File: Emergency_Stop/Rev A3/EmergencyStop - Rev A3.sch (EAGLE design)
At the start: 12 parts, among them J3 NC3FBV2-SW, J4 NC3MAV, J5 22-05-7038-03, J6 22-05-7028-02, T1 EXMACHINA-LOGO-NAME

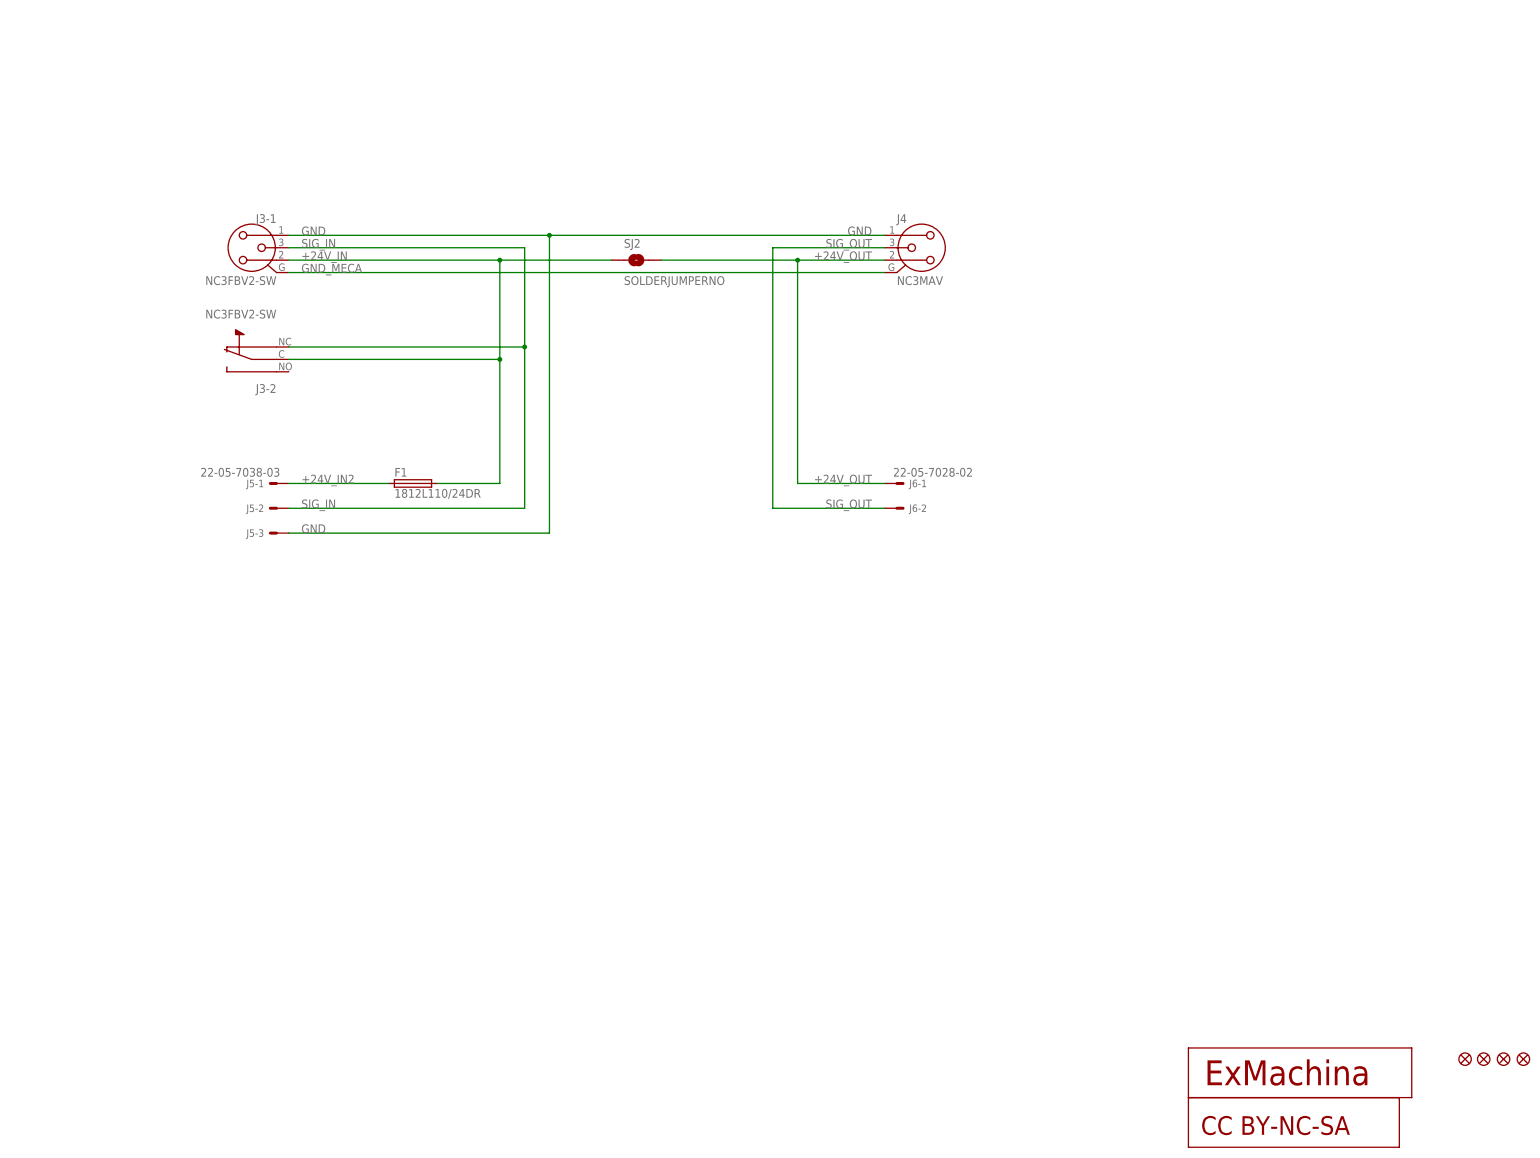
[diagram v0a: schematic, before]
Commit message: Update EmergencyStop - Rev A3
- Fix layout
- Major redesign in schematics
- Add Lamp output
- Add onboard led
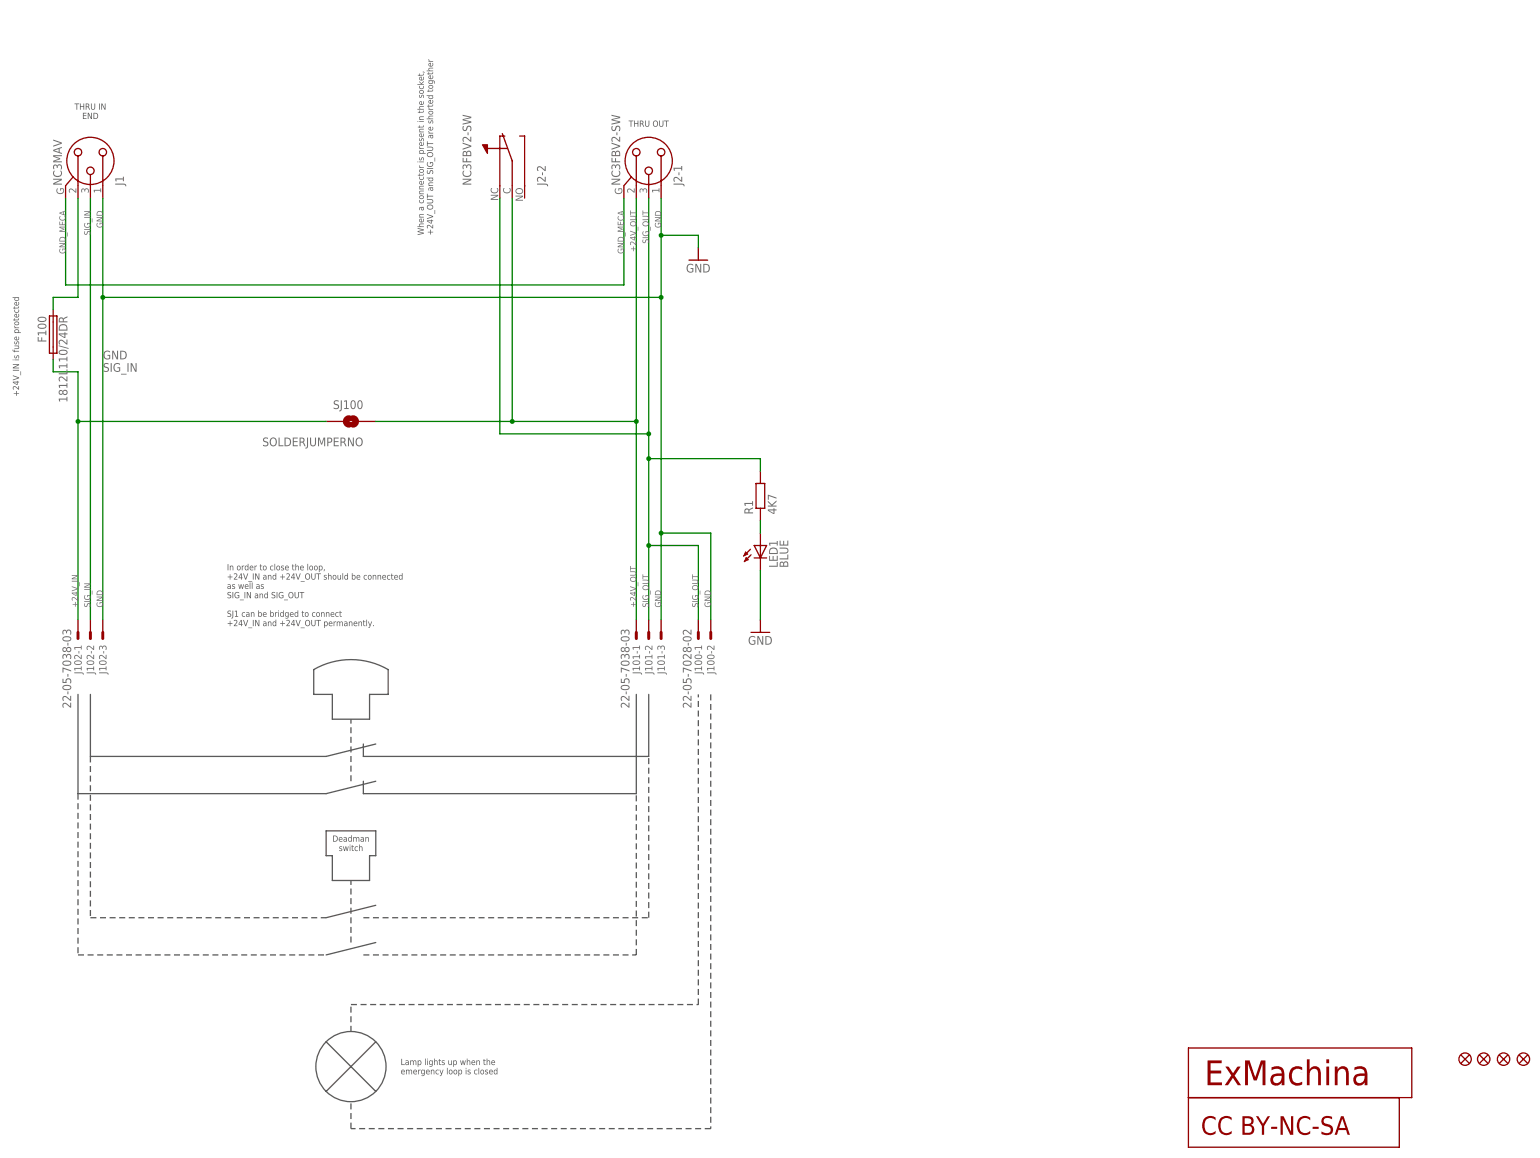
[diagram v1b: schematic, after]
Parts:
- removed F1: 1812L110/24DR, fuse2:1812L110/24DR
- removed J3: NC3FBV2-SW, con-neutrik_ag:NC3FBV2-SW
- removed J4: NC3MAV, con-neutrik_ag:NC3MAV
- removed J5: 22-05-7038-03, con-molex:22-05-7038-03
- removed J6: 22-05-7028-02, con-molex:22-05-7028-02
- removed SJ2: SOLDERJUMPERNO, SparkFun-Passives:SOLDERJUMPERNO
- added F100: 1812L110/24DR, fuse2:1812L110/24DR
- added J1: NC3MAV, con-neutrik_ag:NC3MAV
- added J100: 22-05-7028-02, con-molex:22-05-7028-02
- added J101, J102: 22-05-7038-03, con-molex:22-05-7038-03
- added J2: NC3FBV2-SW, con-neutrik_ag:NC3FBV2-SW
- added LED1: BLUE, led:LEDCHIPLED_0603
- added R1: 4K7, rcl:R-EU_R0603
- added SJ100: SOLDERJUMPERNO, SparkFun-Passives:SOLDERJUMPERNO
- renumbered CC1 to CC100, JP1 to JP100, JP2 to JP103, JP3 to JP102, JP4 to JP101, T1 to T100
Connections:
- removed net +24V_IN2: F1.1, J5-1.S
- new net N$1: F100.1, J1.2
- new net N$2: LED1.A, R1.1
- net +24V_IN: now also F100.2, J102-1.S, SJ100.2; no longer F1.2, J3-1.2, J3-2.N, SJ2.1
- net +24V_OUT: now also J101-1.S, J2-1.2, J2-2.N, SJ100.1; no longer J4.2, J6-1.S, SJ2.2
- net GND: now also J1.1, J100-2.S, J101-3.S, J102-3.S, J2-1.1, LED1.C; no longer J3-1.1, J4.1, J5-3.S
- net GND_MECA: now also J1.G, J2-1.G; no longer J3-1.G, J4.G
- net SIG_IN: now also J1.3, J102-2.S; no longer J3-1.3, J3-2.NC, J5-2.S
- net SIG_OUT: now also J100-1.S, J101-2.S, J2-1.3, J2-2.NC, R1.2; no longer J4.3, J6-2.S
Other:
- note added: "+24V_IN is fuse protected"
- note added: "Deadman switch"
- note added: "In order to close the loop, +24V_IN and +24V_OUT should be connected as well as SIG_IN and SIG_OUT SJ1 can be bridged to connect +24V_IN and +24V_OUT permanently."
- note added: "Lamp lights up when the emergency loop is closed"
- note added: "THRU IN END"
- note added: "THRU OUT"
- note added: "When a connector is present in the socket, +24V_OUT and SIG_OUT are shorted together"

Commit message: Generate MDP files
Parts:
- CC100, J1, J2, JP100, JP101, JP102, JP103, SJ100, T100: OC_NEWARK (none) -> unknown
- F100: MPN (none) -> 1812L110/24DR; OC_NEWARK (none) -> 39X0319
- LED1: MPN (none) -> OVS-0603; OC_NEWARK (none) -> 15R2205
- R1: MPN (none) -> RC0603FR-074K7L; OC_NEWARK (none) -> 68R0092
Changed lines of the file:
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@@
 <parts>
 <part name="FRAME1" library="frames" deviceset="A3L-LOC" device=""/>
-<part name="J1" library="con-neutrik_ag" deviceset="NC3" device="MAV"/>
-<part name="J2" library="con-neutrik_ag" deviceset="NC3?-SW" device="FBV2"/>
-<part name="SJ100" library="SparkFun-Passives" deviceset="SOLDERJUMPER" device="NO"/>
-<part name="F100" library="fuse2" deviceset="1812L" device="" technology="110/24DR"/>
-<part name="CC100" library="cc-by-sa" deviceset="CC-BY-NC-SA" device=""/>
-<part name="T100" library="exmachina" deviceset="EXMACHINA-LOGO" device="-NAME"/>
-<part name="JP100" library="SparkFun" deviceset="FIDUCIAL" device="1X2"/>
-<part name="JP103" library="SparkFun" deviceset="FIDUCIAL" device="1X2"/>
-<part name="JP102" library="SparkFun" deviceset="FIDUCIAL" device="1X2"/>
-<part name="JP101" library="SparkFun" deviceset="FIDUCIAL" device="1X2"/>
+<part name="J1" library="con-neutrik_ag" deviceset="NC3" device="MAV">
+<attribute name="OC_NEWARK" value="unknown"/>
+</part>
+<part name="J2" library="con-neutrik_ag" deviceset="NC3?-SW" device="FBV2">
+<attribute name="MF" value=""/>
+<attribute name="MPN" value=""/>
+<attribute name="OC_NEWARK" value="unknown"/>
+</part>
+<part name="SJ100" library="SparkFun-Passives" deviceset="SOLDERJUMPER" device="NO">
+<attribute name="MF" value=""/>
+<attribute name="MPN" value=""/>
+<attribute name="OC_NEWARK" value="unknown"/>
+</part>
+<part name="F100" library="fuse2" deviceset="1812L" device="" technology="110/24DR">
+<attribute name="MF" value=""/>
+<attribute name="MPN" value="1812L110/24DR"/>
+<attribute name="OC_NEWARK" value="39X0319"/>
+</part>
+<part name="CC100" library="cc-by-sa" deviceset="CC-BY-NC-SA" device="">
+<attribute name="MF" value=""/>
+<attribute name="MPN" value=""/>
+<attribute name="OC_NEWARK" value="unknown"/>
+</part>
+<part name="T100" library="exmachina" deviceset="EXMACHINA-LOGO" device="-NAME">
+<attribute name="MF" value=""/>
+<attribute name="MPN" value=""/>
+<attribute name="OC_NEWARK" value="unknown"/>
+</part>
+<part name="JP100" library="SparkFun" deviceset="FIDUCIAL" device="1X2">
+<attribute name="MF" value=""/>
+<attribute name="MPN" value=""/>
+<attribute name="OC_NEWARK" value="unknown"/>
+</part>
+<part name="JP103" library="SparkFun" deviceset="FIDUCIAL" device="1X2">
+<attribute name="MF" value=""/>
+<attribute name="MPN" value=""/>
+<attribute name="OC_NEWARK" value="unknown"/>
+</part>
+<part name="JP102" library="SparkFun" deviceset="FIDUCIAL" device="1X2">
+<attribute name="MF" value=""/>
+<attribute name="MPN" value=""/>
+<attribute name="OC_NEWARK" value="unknown"/>
+</part>
+<part name="JP101" library="SparkFun" deviceset="FIDUCIAL" device="1X2">
+<attribute name="MF" value=""/>
+<attribute name="MPN" value=""/>
+<attribute name="OC_NEWARK" value="unknown"/>
+</part>
 <part name="J101" library="con-molex" deviceset="22-?-03" device="05-7038"/>
 <part name="J102" library="con-molex" deviceset="22-?-03" device="05-7038"/>
 <part name="J100" library="con-molex" deviceset="22-?-02" device="05-7028"/>
 <part name="GND1" library="supply1" deviceset="GND" device=""/>
-<part name="LED1" library="led" deviceset="LED" device="CHIPLED_0603" value="BLUE"/>
-<part name="R1" library="rcl" deviceset="R-EU_" device="R0603" value="4K7"/>
+<part name="LED1" library="led" deviceset="LED" device="CHIPLED_0603" value="BLUE">
+<attribute name="MF" value=""/>
+<attribute name="MPN" value="OVS-0603"/>
+<attribute name="OC_NEWARK" value="15R2205"/>
+</part>
+<part name="R1" library="rcl" deviceset="R-EU_" device="R0603" value="4K7">
+<attribute name="MF" value=""/>
+<attribute name="MPN" value="RC0603FR-074K7L"/>
+<attribute name="OC_NEWARK" value="68R0092"/>
+</part>
 <part name="GND2" library="supply1" deviceset="GND" device=""/>
 </parts>
@@
 <instance part="FRAME1" gate="G$1" x="0" y="0"/>
 <instance part="J1" gate="G$1" x="63.5" y="205.74" rot="MR90"/>
-<instance part="J2" gate="-1" x="177.8" y="205.74" rot="MR90"/>
+<instance part="J2" gate="-1" x="177.8" y="205.74" rot="MR90">
+<attribute name="OC_NEWARK" x="177.8" y="205.74" size="1.778" layer="96" display="off"/>
+<attribute name="MF" x="177.8" y="205.74" size="1.778" layer="96" display="off"/>
+<attribute name="MPN" x="177.8" y="205.74" size="1.778" layer="96" display="off"/>
+</instance>
 <instance part="J2" gate="-2" x="149.86" y="205.74" rot="MR90"/>
-<instance part="SJ100" gate="1" x="116.84" y="152.4" rot="MR0"/>
-<instance part="F100" gate="G$1" x="55.88" y="170.18" rot="MR270"/>
-<instance part="CC100" gate="G$1" x="303.53" y="8.89"/>
-<instance part="T100" gate="G$1" x="311.15" y="19.05"/>
-<instance part="JP100" gate="G$1" x="344.932" y="21.844"/>
-<instance part="JP103" gate="G$1" x="348.742" y="21.844"/>
-<instance part="JP102" gate="G$1" x="352.806" y="21.844"/>
-<instance part="JP101" gate="G$1" x="356.87" y="21.844"/>
+<instance part="SJ100" gate="1" x="116.84" y="152.4" rot="MR0">
+<attribute name="OC_NEWARK" x="116.84" y="152.4" size="1.778" layer="96" display="off"/>
+<attribute name="MF" x="116.84" y="152.4" size="1.778" layer="96" display="off"/>
+<attribute name="MPN" x="116.84" y="152.4" size="1.778" layer="96" display="off"/>
+</instance>
+<instance part="F100" gate="G$1" x="55.88" y="170.18" rot="MR270">
+<attribute name="OC_NEWARK" x="55.88" y="170.18" size="1.778" layer="96" display="off"/>
+<attribute name="MF" x="55.88" y="170.18" size="1.778" layer="96" display="off"/>
+<attribute name="MPN" x="55.88" y="170.18" size="1.778" layer="96" display="off"/>
+</instance>
+<instance part="CC100" gate="G$1" x="303.53" y="8.89">
+<attribute name="OC_NEWARK" x="303.53" y="8.89" size="1.778" layer="96" display="off"/>
+<attribute name="MF" x="303.53" y="8.89" size="1.778" layer="96" display="off"/>
+<attribute name="MPN" x="303.53" y="8.89" size="1.778" layer="96" display="off"/>
+</instance>
+<instance part="T100" gate="G$1" x="311.15" y="19.05">
+<attribute name="OC_NEWARK" x="311.15" y="19.05" size="1.778" layer="96" display="off"/>
+<attribute name="MF" x="311.15" y="19.05" size="1.778" layer="96" display="off"/>
+<attribute name="MPN" x="311.15" y="19.05" size="1.778" layer="96" display="off"/>
+</instance>
+<instance part="JP100" gate="G$1" x="344.932" y="21.844">
+<attribute name="OC_NEWARK" x="344.932" y="21.844" size="1.778" layer="96" display="off"/>
+<attribute name="MF" x="344.932" y="21.844" size="1.778" layer="96" display="off"/>
+<attribute name="MPN" x="344.932" y="21.844" size="1.778" layer="96" display="off"/>
+</instance>
+<instance part="JP103" gate="G$1" x="348.742" y="21.844">
+<attribute name="OC_NEWARK" x="348.742" y="21.844" size="1.778" layer="96" display="off"/>
+<attribute name="MF" x="348.742" y="21.844" size="1.778" layer="96" display="off"/>
+<attribute name="MPN" x="348.742" y="21.844" size="1.778" layer="96" display="off"/>
+</instance>
+<instance part="JP102" gate="G$1" x="352.806" y="21.844">
+<attribute name="OC_NEWARK" x="352.806" y="21.844" size="1.778" layer="96" display="off"/>
+<attribute name="MF" x="352.806" y="21.844" size="1.778" layer="96" display="off"/>
+<attribute name="MPN" x="352.806" y="21.844" size="1.778" layer="96" display="off"/>
+</instance>
+<instance part="JP101" gate="G$1" x="356.87" y="21.844">
+<attribute name="OC_NEWARK" x="356.87" y="21.844" size="1.778" layer="96" display="off"/>
+<attribute name="MF" x="356.87" y="21.844" size="1.778" layer="96" display="off"/>
+<attribute name="MPN" x="356.87" y="21.844" size="1.778" layer="96" display="off"/>
+</instance>
 <instance part="J101" gate="-1" x="175.26" y="109.22" rot="MR270"/>
 <instance part="J101" gate="-2" x="177.8" y="109.22" rot="R270"/>
@@
 <instance part="J100" gate="-2" x="190.5" y="109.22" rot="MR270"/>
 <instance part="GND1" gate="1" x="187.96" y="185.42"/>
-<instance part="LED1" gate="G$1" x="200.66" y="127"/>
-<instance part="R1" gate="G$1" x="200.66" y="137.16" rot="R90"/>
+<instance part="LED1" gate="G$1" x="200.66" y="127">
+<attribute name="OC_NEWARK" x="200.66" y="127" size="1.778" layer="96" display="off"/>
+<attribute name="MF" x="200.66" y="127" size="1.778" layer="96" display="off"/>
+<attribute name="MPN" x="200.66" y="127" size="1.778" layer="96" display="off"/>
+</instance>
+<instance part="R1" gate="G$1" x="200.66" y="137.16" rot="R90">
+<attribute name="OC_NEWARK" x="200.66" y="137.16" size="1.778" layer="96" display="off"/>
+<attribute name="MF" x="200.66" y="137.16" size="1.778" layer="96" display="off"/>
+<attribute name="MPN" x="200.66" y="137.16" size="1.778" layer="96" display="off"/>
+</instance>
 <instance part="GND2" gate="1" x="200.66" y="109.22"/>
 </instances>
